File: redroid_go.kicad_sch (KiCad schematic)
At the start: 98 parts, among them J1 USB4105-GF-A, J2 5051101892, J3 Conn_01x02_Pin, J4 Conn_01x10_Pin, Q1 UMH3N, Q2 PMOS, Q3 UMH3N, SW1 UP, SW10 A, SW11 SW_SPDT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

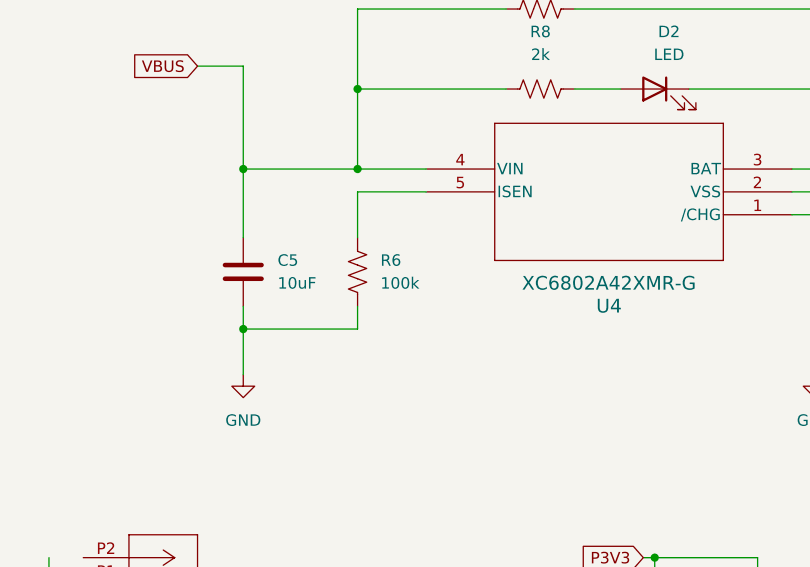
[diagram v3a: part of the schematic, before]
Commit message: Fix ISEN resistor in battery charger
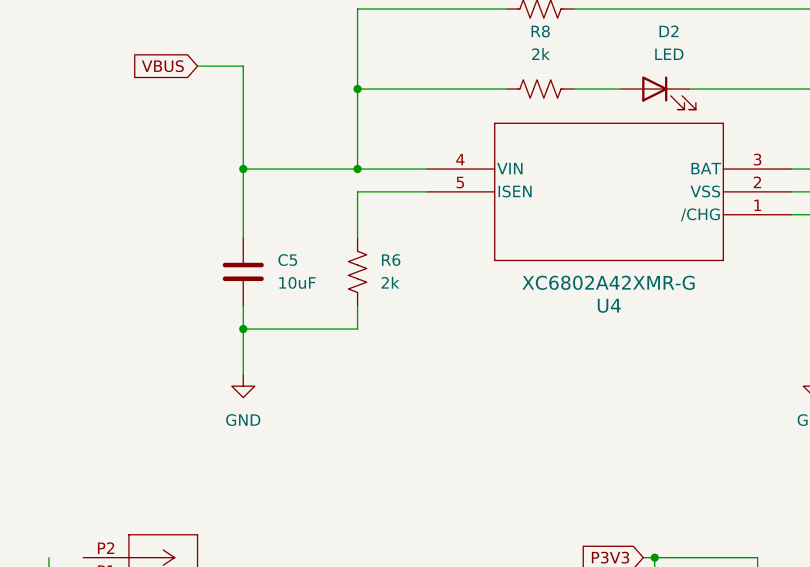
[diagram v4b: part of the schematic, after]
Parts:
- R6: value 100k -> 2k
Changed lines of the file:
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@@
 			)
 		)
-		(property "Value" "100k"
+		(property "Value" "2k"
 			(at 283.21 111.7599 0)
 			(effects

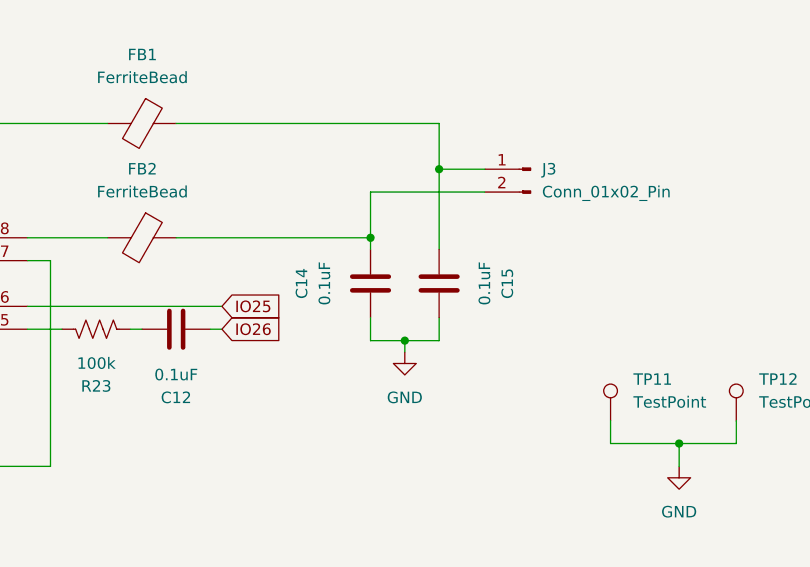
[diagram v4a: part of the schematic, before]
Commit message: Update audio out filter capacitors
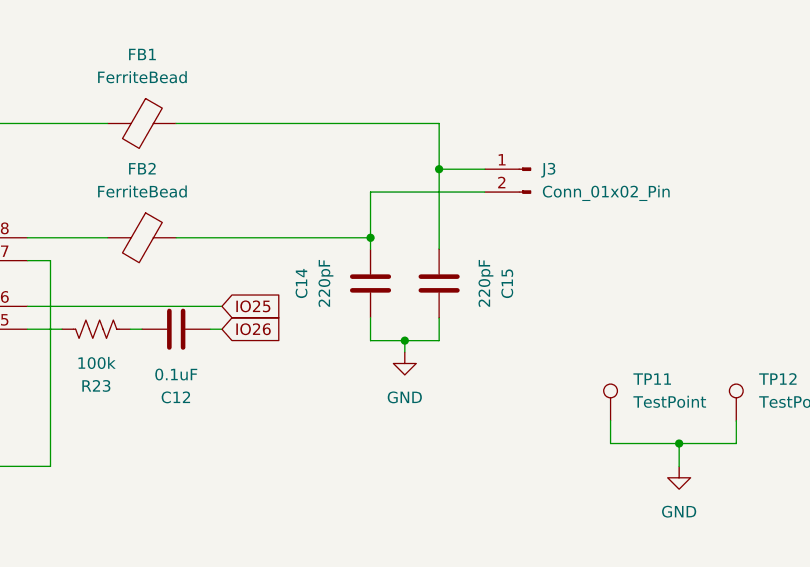
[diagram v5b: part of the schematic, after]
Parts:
- C14, C15: value 0.1uF -> 220pF
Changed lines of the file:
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@@
 			)
 		)
-		(property "Value" "0.1uF"
+		(property "Value" "220pF"
 			(at 132.08 220.98 90)
 			(effects
@@
 			)
 		)
-		(property "Value" "0.1uF"
+		(property "Value" "220pF"
 			(at 114.3 220.98 90)
 			(effects

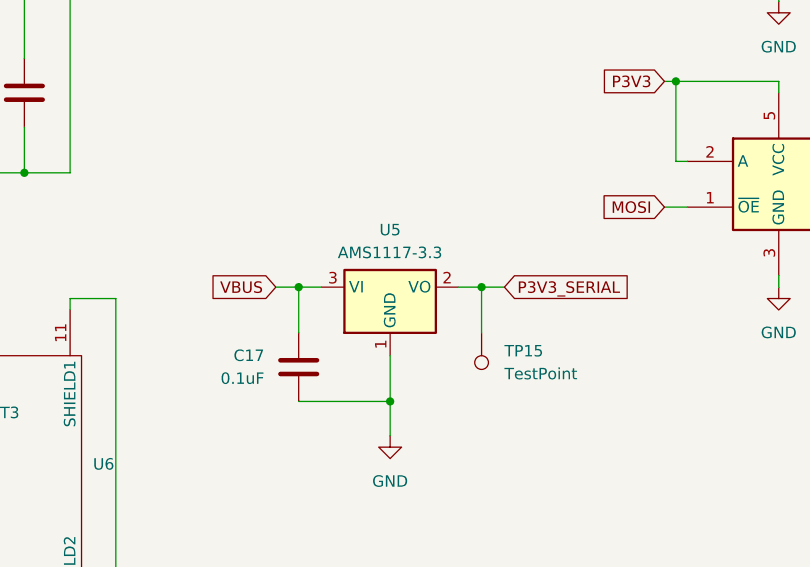
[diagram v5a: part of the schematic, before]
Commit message: Fix 3V3_SERIAL capacitors
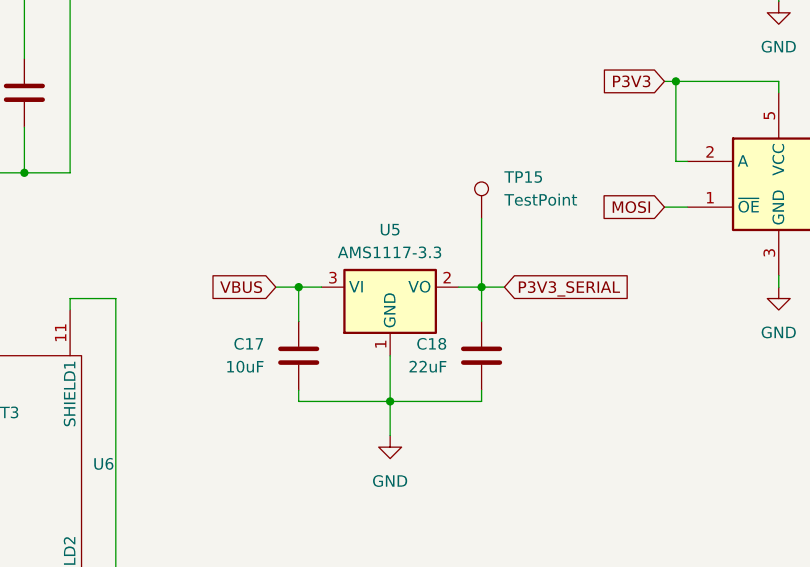
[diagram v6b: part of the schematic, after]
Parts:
- added C18: 22uF, Capacitor_SMD:C_0603_1608Metric_Pad1.08x0.95mm_HandSolder, symbol Device:C
- C17: value 0.1uF -> 10uF
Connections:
- net GND: now also C18.2
- net P3V3_SERIAL: now also C18.1
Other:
- moved on the sheet: C17, TP15
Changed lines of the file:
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@@
 	)
 	(junction
-		(at 177.8 21.59)
+		(at 281.94 240.03)
 		(diameter 0)
 		(color 0 0 0 0)
 	)
 	(junction
-		(at 29.21 162.56)
+		(at 177.8 21.59)
 		(diameter 0)
 		(color 0 0 0 0)
 	)
 	(junction
-		(at 281.94 240.03)
+		(at 29.21 162.56)
 		(diameter 0)
 		(color 0 0 0 0)
@@
 	(wire
 		(pts
-			(xy 281.94 234.95) (xy 281.94 240.03)
-		)
-		(stroke
-			(width 0)
-			(type default)
-		)
-	)
-	(wire
-		(pts
 			(xy 200.66 67.31) (xy 200.66 69.85)
 		)
@@
 	(wire
 		(pts
+			(xy 292.1 227.33) (xy 292.1 231.14)
+		)
+		(stroke
+			(width 0)
+			(type default)
+		)
+	)
+	(wire
+		(pts
 			(xy 46.99 48.26) (xy 71.12 48.26)
 		)
@@
 	(wire
 		(pts
+			(xy 281.94 240.03) (xy 292.1 240.03)
+		)
+		(stroke
+			(width 0)
+			(type default)
+		)
+	)
+	(wire
+		(pts
 			(xy 121.92 144.78) (xy 127 144.78)
 		)
@@
 	(wire
 		(pts
-			(xy 292.1 227.33) (xy 292.1 232.41)
+			(xy 292.1 227.33) (xy 292.1 219.71)
 		)
 		(stroke
@@
 	(wire
 		(pts
-			(xy 281.94 240.03) (xy 281.94 243.84)
-		)
-		(stroke
-			(width 0)
-			(type default)
-		)
-	)
-	(wire
-		(pts
 			(xy 30.48 43.18) (xy 36.83 43.18)
 		)
@@
 	(wire
 		(pts
+			(xy 271.78 240.03) (xy 271.78 238.76)
+		)
+		(stroke
+			(width 0)
+			(type default)
+		)
+	)
+	(wire
+		(pts
 			(xy 224.79 107.95) (xy 213.36 107.95)
 		)
@@
 	(wire
 		(pts
-			(xy 271.78 227.33) (xy 271.78 232.41)
+			(xy 271.78 227.33) (xy 271.78 231.14)
 		)
 		(stroke
@@
 	(wire
 		(pts
+			(xy 281.94 240.03) (xy 281.94 243.84)
+		)
+		(stroke
+			(width 0)
+			(type default)
+		)
+	)
+	(wire
+		(pts
 			(xy 127 163.83) (xy 127 170.18)
 		)
@@
 	(wire
 		(pts
+			(xy 281.94 234.95) (xy 281.94 240.03)
+		)
+		(stroke
+			(width 0)
+			(type default)
+		)
+	)
+	(wire
+		(pts
 			(xy 69.85 142.24) (xy 69.85 144.78)
 		)
@@
 	(wire
 		(pts
+			(xy 292.1 240.03) (xy 292.1 238.76)
+		)
+		(stroke
+			(width 0)
+			(type default)
+		)
+	)
+	(wire
+		(pts
 			(xy 251.46 228.6) (xy 251.46 269.24)
 		)
@@
 	(symbol
 		(lib_id "Device:C")
-		(at 271.78 236.22 0)
+		(at 271.78 234.95 0)
 		(mirror y)
 		(unit 1)
@@
 		(dnp no)
 		(property "Reference" "C17"
-			(at 267.97 234.9499 0)
+			(at 267.97 233.6799 0)
 			(effects
 				(font
@@
 			)
 		)
-		(property "Value" "0.1uF"
-			(at 267.97 237.4899 0)
+		(property "Value" "10uF"
+			(at 267.97 236.2199 0)
 			(effects
 				(font
@@
 		)
 		(property "Footprint" "Capacitor_SMD:C_0603_1608Metric_Pad1.08x0.95mm_HandSolder"
-			(at 270.8148 240.03 0)
+			(at 270.8148 238.76 0)
 			(effects
 				(font
@@
 		)
 		(property "Datasheet" "~"
-			(at 271.78 236.22 0)
+			(at 271.78 234.95 0)
 			(effects
 				(font
@@
 		)
 		(property "Description" "Unpolarized capacitor"
-			(at 271.78 236.22 0)
+			(at 271.78 234.95 0)
 			(effects
 				(font
@@
 	)
 	(symbol
+		(lib_id "Device:C")
+		(at 292.1 234.95 0)
+		(mirror y)
+		(unit 1)
+		(exclude_from_sim no)
+		(in_bom yes)
+		(on_board yes)
+		(dnp no)
+		(property "Reference" "C18"
+			(at 288.29 233.6799 0)
+			(effects
+				(font
+					(size 1.27 1.27)
+				)
+				(justify left)
+			)
+		)
+		(property "Value" "22uF"
+			(at 288.29 236.2199 0)
+			(effects
+				(font
+					(size 1.27 1.27)
+				)
+				(justify left)
+			)
+		)
+		(property "Footprint" "Capacitor_SMD:C_0603_1608Metric_Pad1.08x0.95mm_HandSolder"
+			(at 291.1348 238.76 0)
+			(effects
+				(font
+					(size 1.27 1.27)
+				)
+				(hide yes)
+			)
+		)
+		(property "Datasheet" "~"
+			(at 292.1 234.95 0)
+			(effects
+				(font
+					(size 1.27 1.27)
+				)
+				(hide yes)
+			)
+		)
+		(property "Description" "Unpolarized capacitor"
+			(at 292.1 234.95 0)
+			(effects
+				(font
+					(size 1.27 1.27)
+				)
+				(hide yes)
+			)
+		)
+		(pin "2"
+		)
+		(pin "1"
+		)
+		(instances
+			(project "redroid_go"
+				(path "/54323edd-924e-4c99-bcbf-5375689f8e73"
+					(reference "C18")
+					(unit 1)
+				)
+			)
+		)
+	)
+	(symbol
 		(lib_id "32teeth - Conductive Buttons:CONDUCTIVE_BUTTON_STARTSELECT")
 		(at 116.84 157.48 0)
@@
 	(symbol
 		(lib_id "Connector:TestPoint")
-		(at 292.1 232.41 180)
+		(at 292.1 219.71 0)
 		(unit 1)
 		(exclude_from_sim no)
@@
 		(fields_autoplaced yes)
 		(property "Reference" "TP15"
-			(at 294.64 234.4419 0)
+			(at 294.64 215.1379 0)
 			(effects
 				(font
 					(size 1.27 1.27)
 				)
-				(justify right)
+				(justify left)
 			)
 		)
 		(property "Value" "TestPoint"
-			(at 294.64 236.9819 0)
+			(at 294.64 217.6779 0)
 			(effects
 				(font
 					(size 1.27 1.27)
 				)
-				(justify right)
+				(justify left)
 			)
 		)
 		(property "Footprint" "TestPoint:TestPoint_Pad_D1.5mm"
-			(at 287.02 232.41 0)
+			(at 297.18 219.71 0)
 			(effects
 				(font
@@
 		)
 		(property "Datasheet" "~"
-			(at 287.02 232.41 0)
+			(at 297.18 219.71 0)
 			(effects
 				(font
@@
 		)
 		(property "Description" "test point"
-			(at 292.1 232.41 0)
+			(at 292.1 219.71 0)
 			(effects
 				(font

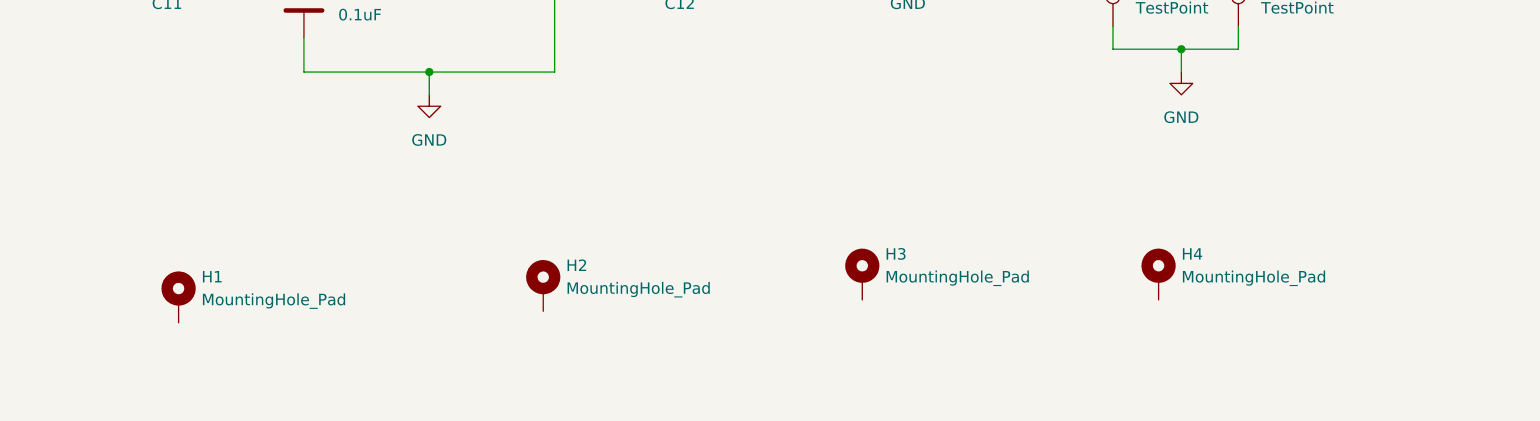
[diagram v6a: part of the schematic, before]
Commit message: Add new mouting hole
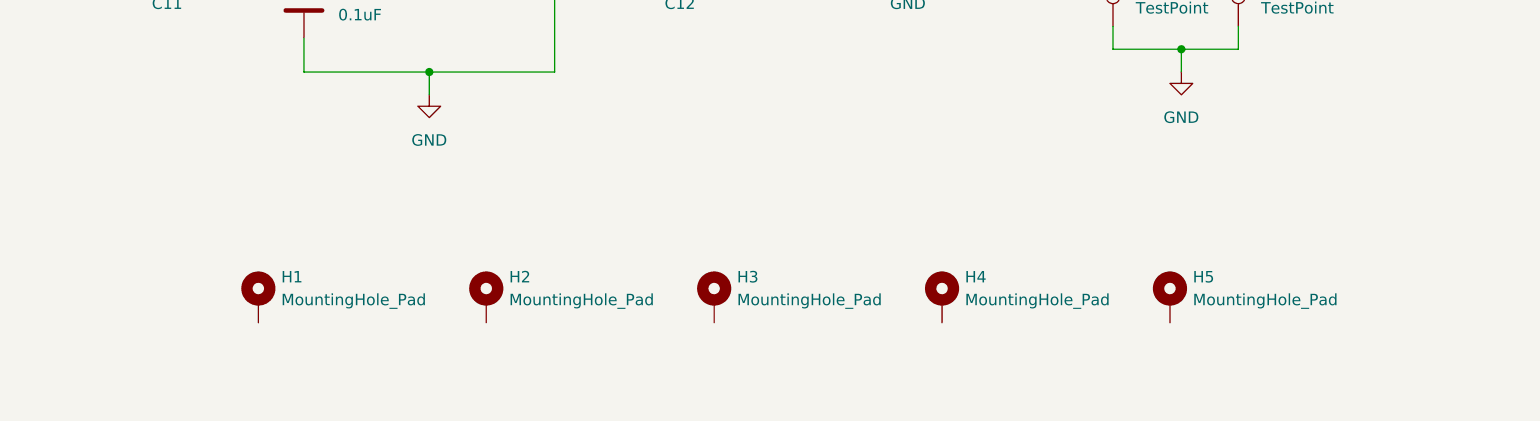
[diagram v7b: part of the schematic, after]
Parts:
- added H5: MountingHole_Pad, MountingHole:MountingHole_2.2mm_M2_DIN965_Pad, symbol Mechanical:MountingHole_Pad
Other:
- moved on the sheet: H1, H2, H3, H4
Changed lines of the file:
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@@
 	(symbol
 		(lib_id "Mechanical:MountingHole_Pad")
-		(at 82.55 265.43 0)
+		(at 76.2 266.7 0)
 		(unit 1)
 		(exclude_from_sim yes)
@@
 		(fields_autoplaced yes)
 		(property "Reference" "H2"
-			(at 85.09 262.8899 0)
+			(at 78.74 264.1599 0)
 			(effects
 				(font
@@
 		)
 		(property "Value" "MountingHole_Pad"
-			(at 85.09 265.4299 0)
+			(at 78.74 266.6999 0)
 			(effects
 				(font
@@
 		)
 		(property "Footprint" "MountingHole:MountingHole_2.2mm_M2_DIN965_Pad"
-			(at 82.55 265.43 0)
+			(at 76.2 266.7 0)
 			(effects
 				(font
@@
 		)
 		(property "Datasheet" "~"
-			(at 82.55 265.43 0)
+			(at 76.2 266.7 0)
 			(effects
 				(font
@@
 		)
 		(property "Description" "Mounting Hole with connection"
-			(at 82.55 265.43 0)
+			(at 76.2 266.7 0)
 			(effects
 				(font
@@
 	(symbol
 		(lib_id "Mechanical:MountingHole_Pad")
-		(at 41.91 266.7 0)
+		(at 50.8 266.7 0)
 		(unit 1)
 		(exclude_from_sim yes)
@@
 		(fields_autoplaced yes)
 		(property "Reference" "H1"
-			(at 44.45 264.1599 0)
+			(at 53.34 264.1599 0)
 			(effects
 				(font
@@
 		)
 		(property "Value" "MountingHole_Pad"
-			(at 44.45 266.6999 0)
+			(at 53.34 266.6999 0)
 			(effects
 				(font
@@
 		)
 		(property "Footprint" "MountingHole:MountingHole_2.2mm_M2_DIN965_Pad"
-			(at 41.91 266.7 0)
+			(at 50.8 266.7 0)
 			(effects
 				(font
@@
 		)
 		(property "Datasheet" "~"
-			(at 41.91 266.7 0)
+			(at 50.8 266.7 0)
 			(effects
 				(font
@@
 		)
 		(property "Description" "Mounting Hole with connection"
-			(at 41.91 266.7 0)
+			(at 50.8 266.7 0)
 			(effects
 				(font
@@
 	(symbol
 		(lib_id "Mechanical:MountingHole_Pad")
-		(at 151.13 264.16 0)
+		(at 127 266.7 0)
 		(unit 1)
 		(exclude_from_sim yes)
@@
 		(fields_autoplaced yes)
 		(property "Reference" "H4"
-			(at 153.67 261.6199 0)
+			(at 129.54 264.1599 0)
 			(effects
 				(font
@@
 		)
 		(property "Value" "MountingHole_Pad"
-			(at 153.67 264.1599 0)
+			(at 129.54 266.6999 0)
 			(effects
 				(font
@@
 		)
 		(property "Footprint" "MountingHole:MountingHole_2.2mm_M2_DIN965_Pad"
-			(at 151.13 264.16 0)
+			(at 127 266.7 0)
 			(effects
 				(font
@@
 		)
 		(property "Datasheet" "~"
-			(at 151.13 264.16 0)
+			(at 127 266.7 0)
 			(effects
 				(font
@@
 		)
 		(property "Description" "Mounting Hole with connection"
-			(at 151.13 264.16 0)
+			(at 127 266.7 0)
 			(effects
 				(font
@@
 	)
 	(symbol
+		(lib_id "Mechanical:MountingHole_Pad")
+		(at 152.4 266.7 0)
+		(unit 1)
+		(exclude_from_sim yes)
+		(in_bom no)
+		(on_board yes)
+		(dnp no)
+		(fields_autoplaced yes)
+		(property "Reference" "H5"
+			(at 154.94 264.1599 0)
+			(effects
+				(font
+					(size 1.27 1.27)
+				)
+				(justify left)
+			)
+		)
+		(property "Value" "MountingHole_Pad"
+			(at 154.94 266.6999 0)
+			(effects
+				(font
+					(size 1.27 1.27)
+				)
+				(justify left)
+			)
+		)
+		(property "Footprint" "MountingHole:MountingHole_2.2mm_M2_DIN965_Pad"
+			(at 152.4 266.7 0)
+			(effects
+				(font
+					(size 1.27 1.27)
+				)
+				(hide yes)
+			)
+		)
+		(property "Datasheet" "~"
+			(at 152.4 266.7 0)
+			(effects
+				(font
+					(size 1.27 1.27)
+				)
+				(hide yes)
+			)
+		)
+		(property "Description" "Mounting Hole with connection"
+			(at 152.4 266.7 0)
+			(effects
+				(font
+					(size 1.27 1.27)
+				)
+				(hide yes)
+			)
+		)
+		(pin "1"
+		)
+		(instances
+			(project "redroid_go"
+				(path "/54323edd-924e-4c99-bcbf-5375689f8e73"
+					(reference "H5")
+					(unit 1)
+				)
+			)
+		)
+	)
+	(symbol
 		(lib_id "power:GND")
 		(at 245.11 271.78 0)
@@
 	(symbol
 		(lib_id "Mechanical:MountingHole_Pad")
-		(at 118.11 264.16 0)
+		(at 101.6 266.7 0)
 		(unit 1)
 		(exclude_from_sim yes)
@@
 		(fields_autoplaced yes)
 		(property "Reference" "H3"
-			(at 120.65 261.6199 0)
+			(at 104.14 264.1599 0)
 			(effects
 				(font
@@
 		)
 		(property "Value" "MountingHole_Pad"
-			(at 120.65 264.1599 0)
+			(at 104.14 266.6999 0)
 			(effects
 				(font
@@
 		)
 		(property "Footprint" "MountingHole:MountingHole_2.2mm_M2_DIN965_Pad"
-			(at 118.11 264.16 0)
+			(at 101.6 266.7 0)
 			(effects
 				(font
@@
 		)
 		(property "Datasheet" "~"
-			(at 118.11 264.16 0)
+			(at 101.6 266.7 0)
 			(effects
 				(font
@@
 		)
 		(property "Description" "Mounting Hole with connection"
-			(at 118.11 264.16 0)
+			(at 101.6 266.7 0)
 			(effects
 				(font

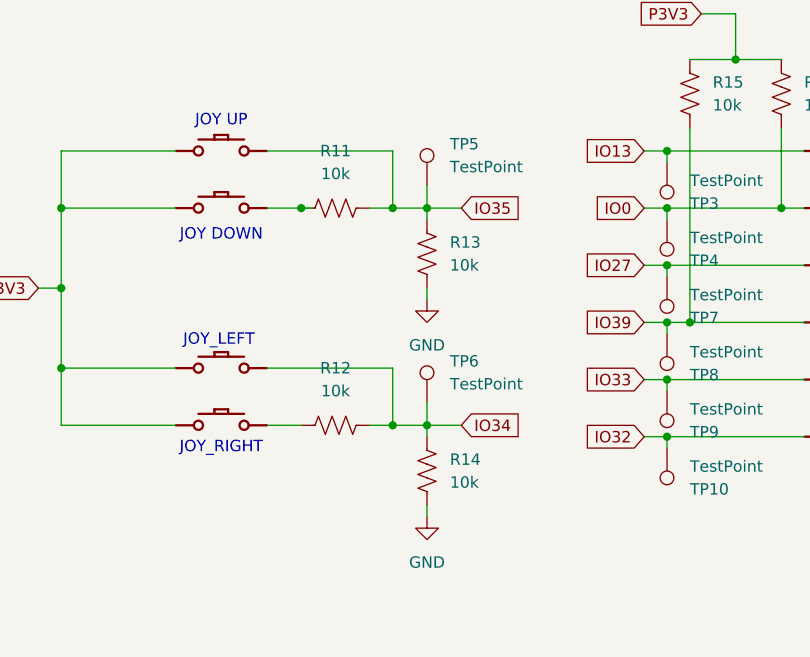
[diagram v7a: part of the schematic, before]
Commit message: Change DPAD resistors
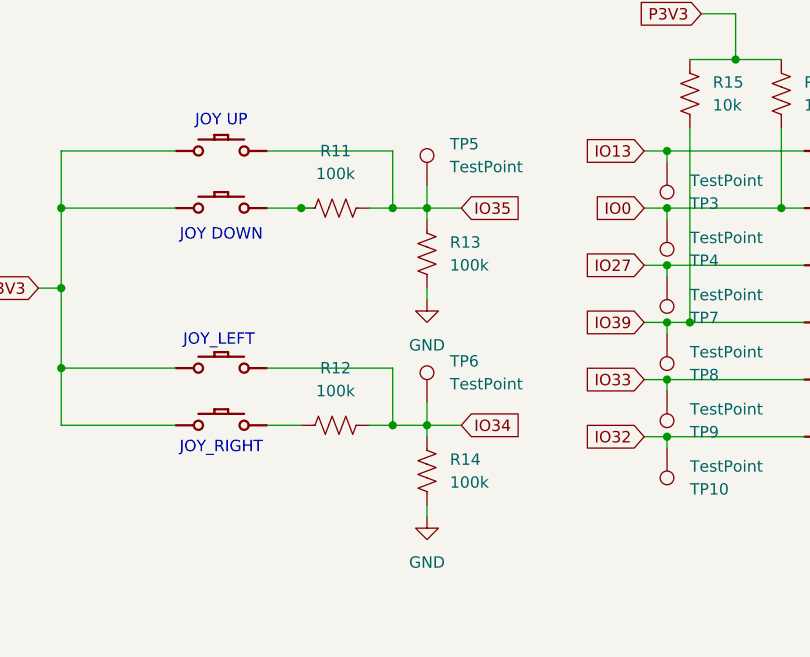
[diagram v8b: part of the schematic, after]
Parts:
- R11, R12, R13, R14: value 10k -> 100k
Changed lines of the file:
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@@
 			)
 		)
-		(property "Value" "10k"
+		(property "Value" "100k"
 			(at 72.39 151.1299 0)
 			(effects
@@
 			)
 		)
-		(property "Value" "10k"
+		(property "Value" "100k"
 			(at 59.69 165.1 90)
 			(effects
@@
 			)
 		)
-		(property "Value" "10k"
+		(property "Value" "100k"
 			(at 72.39 175.2599 0)
 			(effects
@@
 			)
 		)
-		(property "Value" "10k"
+		(property "Value" "100k"
 			(at 59.69 140.97 90)
 			(effects
